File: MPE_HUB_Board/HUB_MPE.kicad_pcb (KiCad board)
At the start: 4 copper layers, 132 x 118.7 mm, 230 parts, among them J1 Conn_01x09, J2 Conn_01x03, J3 Conn_01x06, J4 Conn_01x07, J5 Conn_01x05, J6 Conn_01x05, J7 PZ254-1-04-Z-2.5-G1, Q1 IRLML0100TRPBF, Q10 AO3400A, Q11 AO3400A, Q2 AO3400A, Q3 AO3400A, Q4 AO3400A, Q5 AO3400A, Q6 AO3400A, Q7 AO3400A, Q8 AO3400A, Q9 AO3400A, T1 H1102NLT, T2 H1102NLT, T3 H1102NLT, T4 H1102NLT, T6 H1102NLT, U1 K7803M-1000R3_C2916516, U2 RTL8305NB-VB-CG, U3 MAX3485ESA, U4 ESP32-S3-MINI-1-N4R2, U5 VND7050AJTR, U6 VND7050AJTR, U7 W5500, X1 25Mhz, X2 25MHz

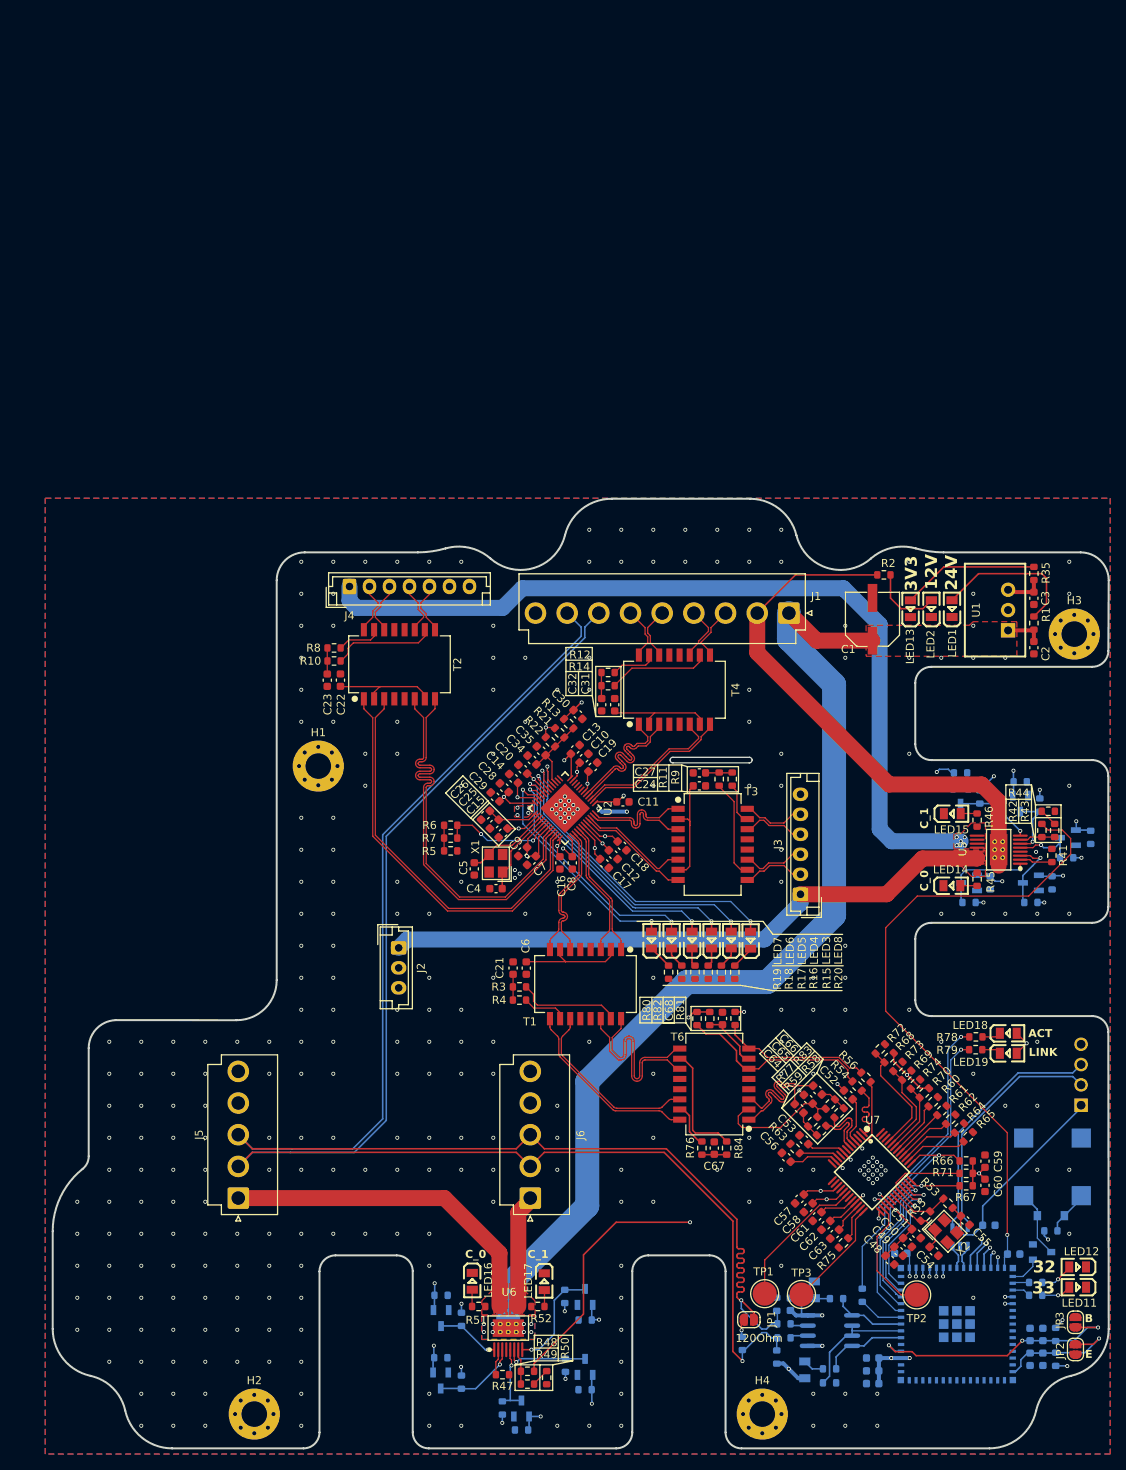
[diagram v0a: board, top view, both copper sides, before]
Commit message: Riadattamento dimensioni scheda
Offset verso l'interno di 1 mm per ingombri meccanici
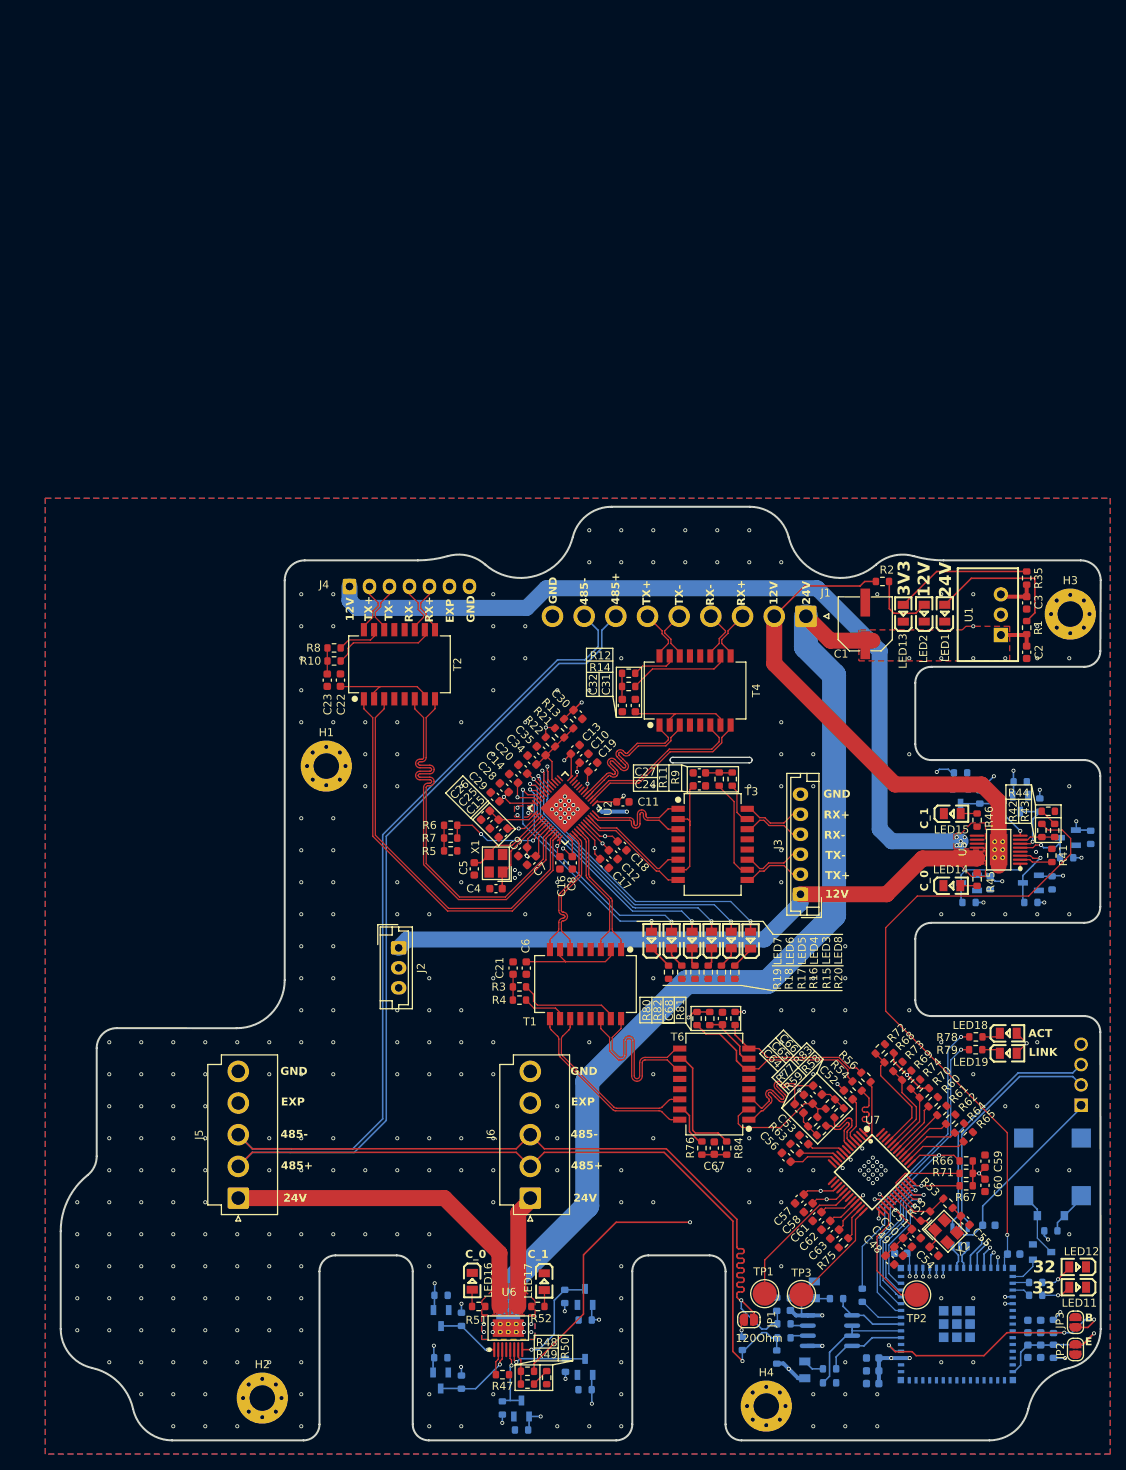
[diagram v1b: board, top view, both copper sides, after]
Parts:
- moved R12 2.58 mm to (99.8, 42.4)
- moved C31 2.58 mm to (100.6, 46.4)
- moved R14 2.58 mm to (99.8, 44.0)
- moved C32 2.58 mm to (99.0, 46.4)
- moved T4 2.58 mm to (108.1, 44.5)
- moved H3 2.55 mm to (155.0, 35.0)
- moved H2 2.24 mm to (54.0, 133.0)
- moved J1 2.16 mm to (122.0, 35.3)
- moved H4 1.12 mm to (117.0, 134.0)
- moved C1 1.07 mm to (129.4, 36.2)
- moved C3 1.07 mm to (149.5, 33.6)
- moved LED1 1.07 mm to (139.3, 34.9)
- moved U1 1.07 mm to (146.3, 35.1)
- moved LED13 1.07 mm to (134.1, 34.9)
- moved LED2 1.07 mm to (136.7, 34.9)
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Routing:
- net /MCU_ESP32/BOOT: track 32.8 -> 37.3 mm
- net +12V: track 67.8 -> 63.7 mm
- net +24V: track 130.6 -> 127.0 mm
- net /Switch/TXOP3: track 18.7 -> 21.7 mm
- net /Switch/TXON3: track 19.0 -> 21.9 mm
- net /Switch/RXIP3: track 19.1 -> 21.8 mm
- net /Switch/RXIN3: track 18.9 -> 21.6 mm
- net /485_ROV+: track 189.4 -> 191.9 mm
- net /485_ROV-: track 191.6 -> 194.0 mm
- net /+12V_BD3D: track 107.7 -> 105.7 mm
- net Net-(LED2-+): track 9.00 -> 7.94 mm
- net GND: vias 299 -> 303
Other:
- board size 132 x 118.7 mm -> 130 x 116.7 mm
- board text added: "485+"
- board text added: "485-"
- board text added: "EXP"
- board text added: "GND"
- board text added: "RX+"
- board text added: "RX-"
- board text added: "TX+"
- board text added: "TX-"

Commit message: Primo Firmware MPE_HUB
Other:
- board text added: "36"
- board text added: "37"
- board text added: "PWM"
- board text removed: "32"
- board text removed: "33"
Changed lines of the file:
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@@
 			(psa4output no)
 			(plot_black_and_white yes)
-			(plotinvisibletext no)
 			(sketchpadsonfab no)
 			(plotpadnumbers no)
@@
 		(tags "connector JST EH vertical")
 		(property "Reference" "J2"
-			(at 2.5 -2.8 90)
+			(at 2.5 -3.35 90)
 			(layer "F.SilkS")
 			(effects
@@
 		)
 	)
+	(gr_text "GND"
+		(at 64.7 82.5 0)
+		(layer "F.SilkS")
+		(effects
+			(font
+				(size 1 1)
+				(thickness 0.25)
+				(bold yes)
+			)
+			(justify left bottom)
+		)
+	)
 	(gr_text "485-"
 		(at 92.525 100.6 0)
@@
 		)
 	)
+	(gr_text "24V"
+		(at 64.8 77.3 0)
+		(layer "F.SilkS")
+		(effects
+			(font
+				(size 1 1)
+				(thickness 0.25)
+				(bold yes)
+			)
+			(justify left bottom)
+		)
+	)
 	(gr_text "C_0"
 		(at 137.35 69.65 90)
@@
 		)
 	)
+	(gr_text "PWM"
+		(at 64.7 80 0)
+		(layer "F.SilkS")
+		(effects
+			(font
+				(size 1 1)
+				(thickness 0.25)
+				(bold yes)
+			)
+			(justify left bottom)
+		)
+	)
 	(gr_text "3V3"
 		(at 135.099999 32.725 90)
@@
 		)
 	)
-	(gr_text "32"
+	(gr_text "37"
 		(at 150.325 117.475 0)
 		(layer "F.SilkS")
@@
 		)
 	)
-	(gr_text "33"
+	(gr_text "36"
 		(at 150.225 120.1 0)
 		(layer "F.SilkS")

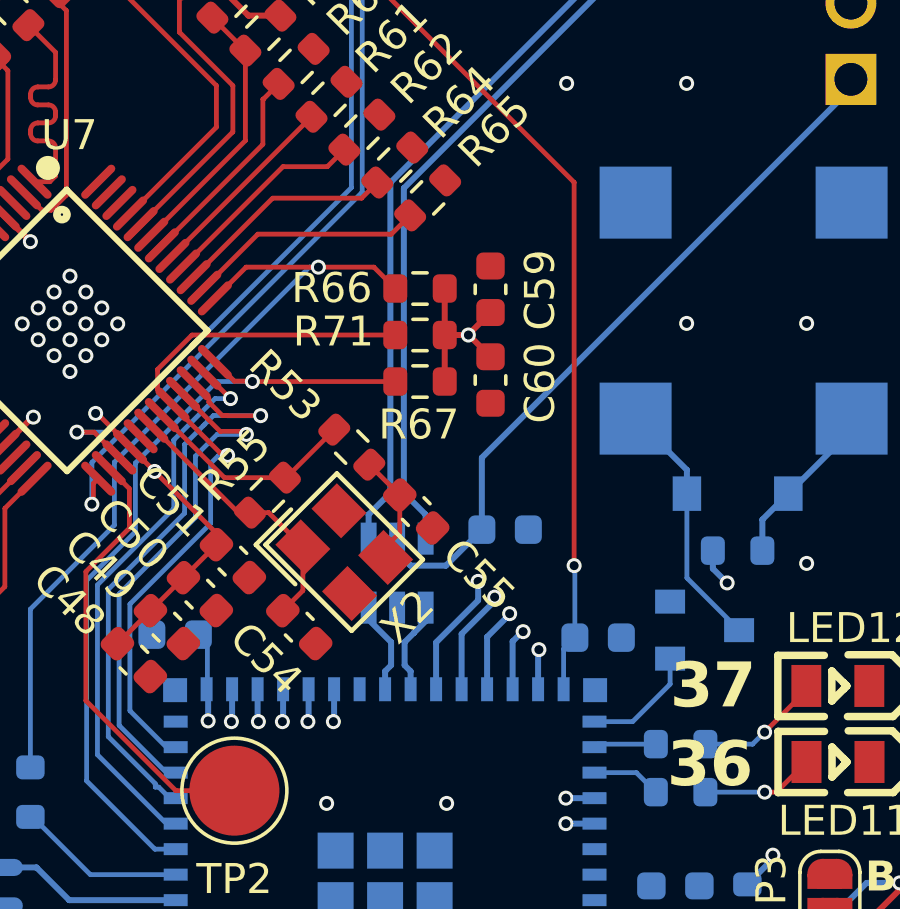
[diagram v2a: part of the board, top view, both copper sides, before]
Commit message: Implementazione server e richieste POST/GET
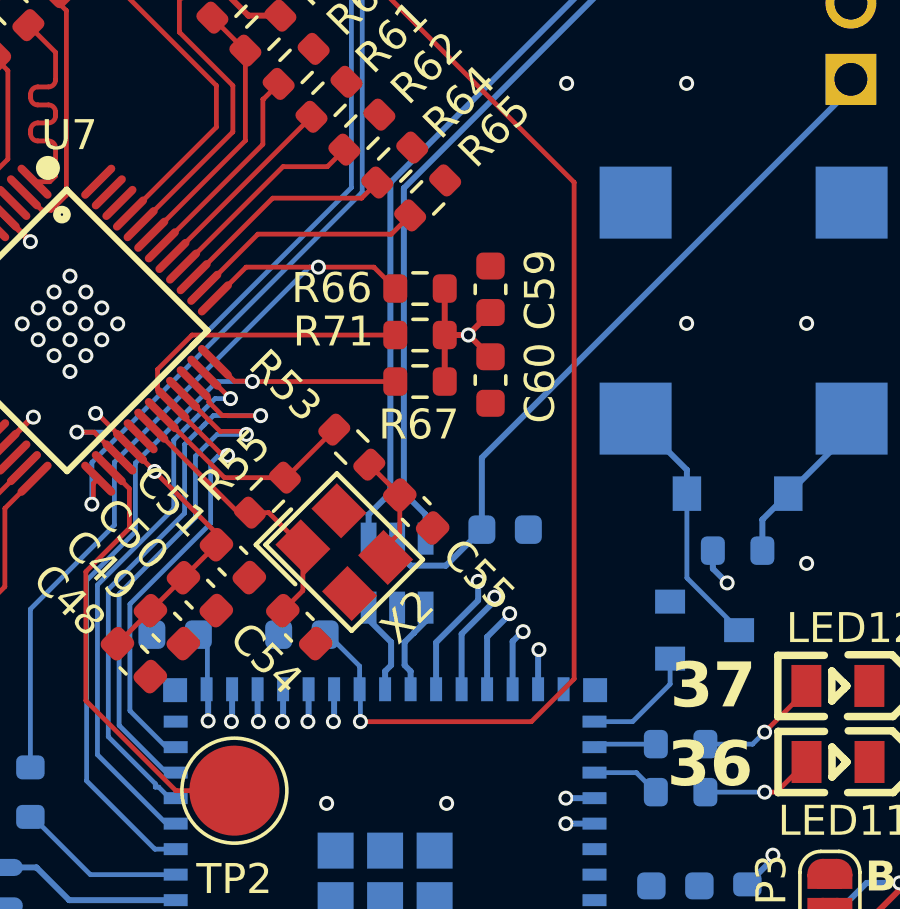
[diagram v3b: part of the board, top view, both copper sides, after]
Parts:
- moved C39 9.87 mm to (138.1, 114.9), turned to 0 degrees
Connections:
- U4 pad 22: unconnected-(U4-IO18-Pad22) -> /+12V_MULTISENSE
- U4 pad 30: /+12V_MULTISENSE -> unconnected-(U4-IO48-Pad30)
- U5 pad : +12V -> (no net)
- U6 pad : +24V -> (no net)
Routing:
- net /+12V_MULTISENSE: track 82.2 -> 92.7 mm

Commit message: Update 08/07/2025
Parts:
- removed J7: PZ254-1-04-Z-2.5-G1, easyeda2kicad:HDR-TH_4P-P2.54-V-M
- removed Q10, Q11, Q2, Q3, Q4, Q5, Q6, Q7, Q8, Q9: AO3400A, easyeda2kicad:SOT-23-3_L2.9-W1.3-P1.90-LS2.4-BR
- removed R102, R104: 10k, Resistor_SMD:R_0603_1608Metric
- removed R103: 15k, Resistor_SMD:R_0603_1608Metric
- added C69: 100nf, Capacitor_SMD:C_0603_1608Metric, F.Cu at (25.5, -35.0)
- added C70: 100nf, Capacitor_SMD:C_0603_1608Metric, F.Cu at (25.5, -32.5)
- added C71: 100nf, Capacitor_SMD:C_0603_1608Metric, F.Cu at (25.5, -30.0)
- added JP4: SolderJumper_2_Open, Jumper:SolderJumper-2_P1.3mm_Open_RoundedPad1.0x1.5mm, F.Cu at (33.7, -34.5)
- added JP5: SolderJumper_2_Open, Jumper:SolderJumper-2_P1.3mm_Open_RoundedPad1.0x1.5mm, F.Cu at (33.7, -30.9)
- added LED20: 0805_RED, easyeda2kicad:LED0805-R-RD, F.Cu at (26.3, -19.5)
- added LED21: 0805_GREEN, easyeda2kicad:LED0805-R-RD, F.Cu at (26.3, -16.2)
- added LED22: 0805_RED, easyeda2kicad:LED0805-R-RD, F.Cu at (26.3, -12.9)
- added LED23: 0805_GREEN, easyeda2kicad:LED0805-R-RD, F.Cu at (26.3, -9.61)
- added R105: 1K, Resistor_SMD:R_0603_1608Metric, F.Cu at (25.5, -22.4)
- added R106: 100k, Resistor_SMD:R_0603_1608Metric, F.Cu at (29.5, -35.0)
- added R107: 1K, Resistor_SMD:R_0603_1608Metric, F.Cu at (29.5, -32.5)
- added R108: CRCW060310R0JNEAHP, easyeda2kicad:R0603, F.Cu at (43.8, -16.0)
- added R109: CRCW060310R0JNEAHP, easyeda2kicad:R0603, F.Cu at (43.8, -13.6)
- added R110: 10K, Resistor_SMD:R_0603_1608Metric, F.Cu at (29.5, -30.0)
- added R111: 120, Resistor_SMD:R_0603_1608Metric, F.Cu at (29.5, -27.5)
- added R112: 10K, Resistor_SMD:R_0603_1608Metric, F.Cu at (29.5, -24.9)
- added R37: 5.1k, Resistor_SMD:R_0603_1608Metric, B.Cu at (148.2, 90.4)
- added R38: 5.1k, Resistor_SMD:R_0603_1608Metric, B.Cu at (151.3, 98.0)
- added TP4: TestPoint_Probe, easyeda2kicad:TEST-TH_BD2.54-P1.39, F.Cu at (113.5, 26.1)
- added TP5: TestPoint_Probe, easyeda2kicad:TEST-TH_BD2.54-P1.39, F.Cu at (106.4, 26.0)
- added TP6: TestPoint_Probe, easyeda2kicad:TEST-TH_BD2.54-P1.39, F.Cu at (99.3, 26.0)
- added U10: MAX3485ESA, easyeda2kicad:SOP-8_L5.0-W4.0-P1.27-LS6.0-BL, F.Cu at (45.8, -32.0)
- added U8: MAX3485ESA, easyeda2kicad:SOP-8_L5.0-W4.0-P1.27-LS6.0-BL, F.Cu at (39.3, -32.0)
- added U9: ADS1015IDGSR, easyeda2kicad:VSSOP-10_L3.0-W3.0-P0.50-LS4.9-BL, F.Cu at (43.5, -22.1)
- added USB2: TYPEC-303-ACP16, easyeda2kicad:USB-C-SMD_TYPEC-303-ACP16, F.Cu at (149.8, 94.2)
- J2: footprint Connector_JST:JST_EH_B3B-EH-A_1x03_P2.50mm_Vertical -> Connector_JST:JST_VH_B3P-VH_1x03_P3.96mm_Vertical
- J3: footprint Connector_JST:JST_EH_B6B-EH-A_1x06_P2.50mm_Vertical -> Connector_JST:JST_VH_B6P-VH-B_1x06_P3.96mm_Vertical
- J4: footprint Connector_JST:JST_EH_B7B-EH-A_1x07_P2.50mm_Vertical -> Connector_JST:JST_VH_B7P-VH-B_1x07_P3.96mm_Vertical
- LED2: value 0805_RED -> 0805_YELLOW
- R100, R88, R98: value 10k -> 15k
- R26, R31: value 0 -> CRCW060310R0JNEAHP; footprint Resistor_SMD:R_0603_1608Metric -> easyeda2kicad:R0603
- R28: value 300 -> 1K
- R30: value 220 -> 1K
- R43, R49: value 330 -> 1K
- R85, R89, R95, R97: value 15k -> 10K
- R86: value 10k -> 10K
- R90, R92: value 10k -> 1K
- R91: value 15k -> 100k
- R93: value 15k -> CRCW060310R0JNEAHP; footprint Resistor_SMD:R_0603_1608Metric -> easyeda2kicad:R0603
- R94: value 10k -> CRCW060310R0JNEAHP; footprint Resistor_SMD:R_0603_1608Metric -> easyeda2kicad:R0603
- R96: value 10k -> 120
- moved C40 1.04 mm to (144.3, 110.5), turned to 90 degrees
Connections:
- C38 pad 2: /+24V_MULTISENSE -> /+12V_MULTISENSE
- C39 pad 2: /+12V_MULTISENSE -> /+24V_MULTISENSE
- C40 pad 1: GND -> /MCU_ESP32/USB_VBUS
- C40 pad 2: /MCU_ESP32/USB_VBUS -> GND
- J5 pad 2: /485_ROV+ -> /485_LED1_+
- J5 pad 3: /485_ROV- -> /485_LED1_-
- J6 pad 2: /485_ROV+ -> /485_LED2_+
- J6 pad 3: /485_ROV- -> /485_LED2_-
- JP1 pad 2: /485_ROV- -> /485_LED2_-
- R100 pad 2: /MCU_ESP32/12V_EC_1 -> Net-(R100-Pad2)
- R101 pad 1: /Power_Switch1/MOSFET_CTRL4/OUTPUT -> GND
- R101 pad 2: +3.3V -> Net-(R101-Pad2)
- R25 pad 2: /485_ROV- -> /485_LED2_-
- R26 pad 2: /485_ROV- -> /485_LED2_-
- R27 pad 2: /485_ROV+ -> /485_LED2_+
- R28 pad 1: /MCU_ESP32/RX2_485 -> Net-(LED9--)
- R28 pad 2: Net-(LED9--) -> /MCU_ESP32/RX3_485_LED2
- R29 pad 1: /MCU_ESP32/R/W_485 -> /MCU_ESP32/R/W_485_LED2
- R30 pad 1: /MCU_ESP32/TX2_485 -> Net-(LED10-K)
- R30 pad 2: Net-(LED10-K) -> /MCU_ESP32/TX3_485_LED2
- R31 pad 2: /485_ROV+ -> /485_LED2_+
- R32 pad 1: /485_ROV+ -> /485_LED2_+
- R85 pad 1: /Power_Switch/MOSFET_CTRL/OUTPUT -> +3.3V
- R85 pad 2: +3.3V -> /MCU_ESP32/SDA
- R86 pad 1: GND -> +3.3V
- R86 pad 2: /MCU_ESP32/12V_EC_0 -> /MCU_ESP32/SDA
- R87 pad 1: /Power_Switch/MOSFET_CTRL1/OUTPUT -> +3.3V
- R87 pad 2: +3.3V -> Net-(U5-SEn)
- R88 pad 1: GND -> +3.3V
- R88 pad 2: /MCU_ESP32/12V_SE -> Net-(U6-SEn)
- R89 pad 1: /Power_Switch1/MOSFET_CTRL1/OUTPUT -> +3.3V
- R89 pad 2: +3.3V -> /MCU_ESP32/CONV_RDY
- R90 pad 1: GND -> Net-(LED22--)
- R90 pad 2: /MCU_ESP32/24V_SE -> /MCU_ESP32/RX2_485_LED1
- R91 pad 1: /Power_Switch/MOSFET_CTRL2/OUTPUT -> /MCU_ESP32/R/W_485_LED1
- R91 pad 2: +3.3V -> GND
- R92 pad 1: GND -> Net-(LED23-K)
- R92 pad 2: /MCU_ESP32/12V_SEL_0 -> /MCU_ESP32/TX2_485_LED1
- R93 pad 1: /Power_Switch1/MOSFET_CTRL2/OUTPUT -> Net-(U10-B)
- R93 pad 2: +3.3V -> /485_LED1_-
- R94 pad 1: GND -> Net-(U10-A)
- R94 pad 2: /MCU_ESP32/24V_SEL_0 -> /485_LED1_+
- R95 pad 1: /Power_Switch/MOSFET_CTRL3/OUTPUT -> GND
- R95 pad 2: +3.3V -> /485_LED1_-
- R96 pad 1: GND -> Net-(JP5-A)
- R96 pad 2: /MCU_ESP32/12V_SEL_1 -> /485_LED1_+
- R97 pad 1: /Power_Switch1/MOSFET_CTRL3/OUTPUT -> /485_LED1_+
- R98 pad 1: GND -> Net-(R100-Pad2)
- R98 pad 2: /MCU_ESP32/24V_SEL_1 -> /+12V_MULTISENSE
- R99 pad 1: /Power_Switch/MOSFET_CTRL4/OUTPUT -> Net-(R101-Pad2)
- R99 pad 2: +3.3V -> /+24V_MULTISENSE
- U3 pad 1: /MCU_ESP32/RX2_485 -> /MCU_ESP32/RX3_485_LED2
- U3 pad 2: /MCU_ESP32/R/W_485 -> /MCU_ESP32/R/W_485_LED2
- U3 pad 3: /MCU_ESP32/R/W_485 -> /MCU_ESP32/R/W_485_LED2
- U3 pad 4: /MCU_ESP32/TX2_485 -> /MCU_ESP32/TX3_485_LED2
- U4 pad 15: unconnected-(U4-IO11-Pad15) -> /MCU_ESP32/TX3_485_LED2
- U4 pad 16: /+24V_MULTISENSE -> /MCU_ESP32/R/W_485_LED2
- U4 pad 17: /MCU_ESP32/24V_EC_0 -> /MCU_ESP32/RX3_485_LED2
- U4 pad 18: /MCU_ESP32/24V_SE -> /MCU_ESP32/24V_EC_0
- U4 pad 22: /+12V_MULTISENSE -> /MCU_ESP32/12V_EC_1
- U4 pad 26: /MCU_ESP32/12V_SE -> unconnected-(U4-IO26-Pad26)
- U4 pad 29: /MCU_ESP32/12V_EC_1 -> /MCU_ESP32/SDA
- U4 pad 30: unconnected-(U4-IO48-Pad30) -> /MCU_ESP32/SCL
- U4 pad 36: unconnected-(U4-IO40-Pad36) -> /MCU_ESP32/RX1_485_ROV
- U4 pad 37: unconnected-(U4-IO41-Pad37) -> /MCU_ESP32/R/W_485_ROV
- U4 pad 38: unconnected-(U4-IO42-Pad38) -> /MCU_ESP32/TX1_485_ROV
- U4 pad 5: unconnected-(U4-IO1-Pad5) -> /MCU_ESP32/CONV_RDY
- U4 pad 6: /MCU_ESP32/TX2_485 -> /MCU_ESP32/TX2_485_LED1
- U4 pad 7: /MCU_ESP32/R/W_485 -> /MCU_ESP32/R/W_485_LED1
- U4 pad 8: /MCU_ESP32/RX2_485 -> /MCU_ESP32/RX2_485_LED1
- U5 pad 1: /Power_Switch/MOSFET_CTRL/OUTPUT -> /MCU_ESP32/12V_EC_0
- U5 pad 3: /Power_Switch/MOSFET_CTRL1/OUTPUT -> Net-(U5-SEn)
- U5 pad 5: /Power_Switch/MOSFET_CTRL2/OUTPUT -> /MCU_ESP32/12V_SEL_0
- U5 pad 6: /Power_Switch/MOSFET_CTRL3/OUTPUT -> /MCU_ESP32/12V_SEL_1
- U5 pad 8: /Power_Switch/MOSFET_CTRL4/OUTPUT -> /MCU_ESP32/12V_EC_1
- U6 pad 1: /Power_Switch1/MOSFET_CTRL/OUTPUT -> /MCU_ESP32/24V_EC_0
- U6 pad 3: /Power_Switch1/MOSFET_CTRL1/OUTPUT -> Net-(U6-SEn)
- U6 pad 5: /Power_Switch1/MOSFET_CTRL2/OUTPUT -> /MCU_ESP32/24V_SEL_0
- U6 pad 6: /Power_Switch1/MOSFET_CTRL3/OUTPUT -> /MCU_ESP32/24V_SEL_1
- U6 pad 8: /Power_Switch1/MOSFET_CTRL4/OUTPUT -> /MCU_ESP32/24V_EC_1
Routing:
- net /485_ROV-: track 194.0 -> 0.00 mm, vias 1 -> 0
- net /485_ROV+: track 191.9 -> 0.00 mm, vias 1 -> 0
- net /RESET_SWITCH: track 112.5 -> 1.58 mm, vias 2 -> 0
- net /+12V_BD3D: track 105.7 -> 0.00 mm, vias 5 -> 0
- net +24V: track 127.0 -> 26.9 mm
- net /PWM_LIGHT: track 94.1 -> 0.00 mm, vias 1 -> 0
- net /+12V_MULTISENSE: track 92.7 -> 0.00 mm, vias 1 -> 0
- net /MCU_ESP32/12V_SEL_0: track 90.7 -> 0.00 mm, vias 2 -> 0
- net /MCU_ESP32/12V_SEL_1: track 86.8 -> 0.00 mm, vias 2 -> 0
- net /MCU_ESP32/24V_SE: track 82.6 -> 0.00 mm, vias 2 -> 0
- net /MCU_ESP32/12V_SE: track 81.6 -> 0.00 mm, vias 2 -> 0
- net /MCU_ESP32/12V_EC_1: track 79.4 -> 0.00 mm, vias 2 -> 0
- net /MCU_ESP32/24V_SEL_0: track 77.4 -> 0.00 mm, vias 2 -> 0
- net /MCU_ESP32/24V_SEL_1: track 74.7 -> 0.00 mm, vias 2 -> 0
- net /MCU_ESP32/24V_EC_0: track 74.5 -> 0.00 mm, vias 2 -> 0
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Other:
- board text added: "HUB_MPE_V1.1_48315"
- board text removed: "HUB_MPE_V1.0_48315"
